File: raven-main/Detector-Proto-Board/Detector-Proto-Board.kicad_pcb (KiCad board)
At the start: 2 copper layers, 40.2 x 40.4 mm, 41 parts, among them IC1 ADA4817-1ARDZ-R7, J1 Conn_01x04, J2 Conn_01x01, J3 Conn_01x02, U9 TLV3201AIDCKT

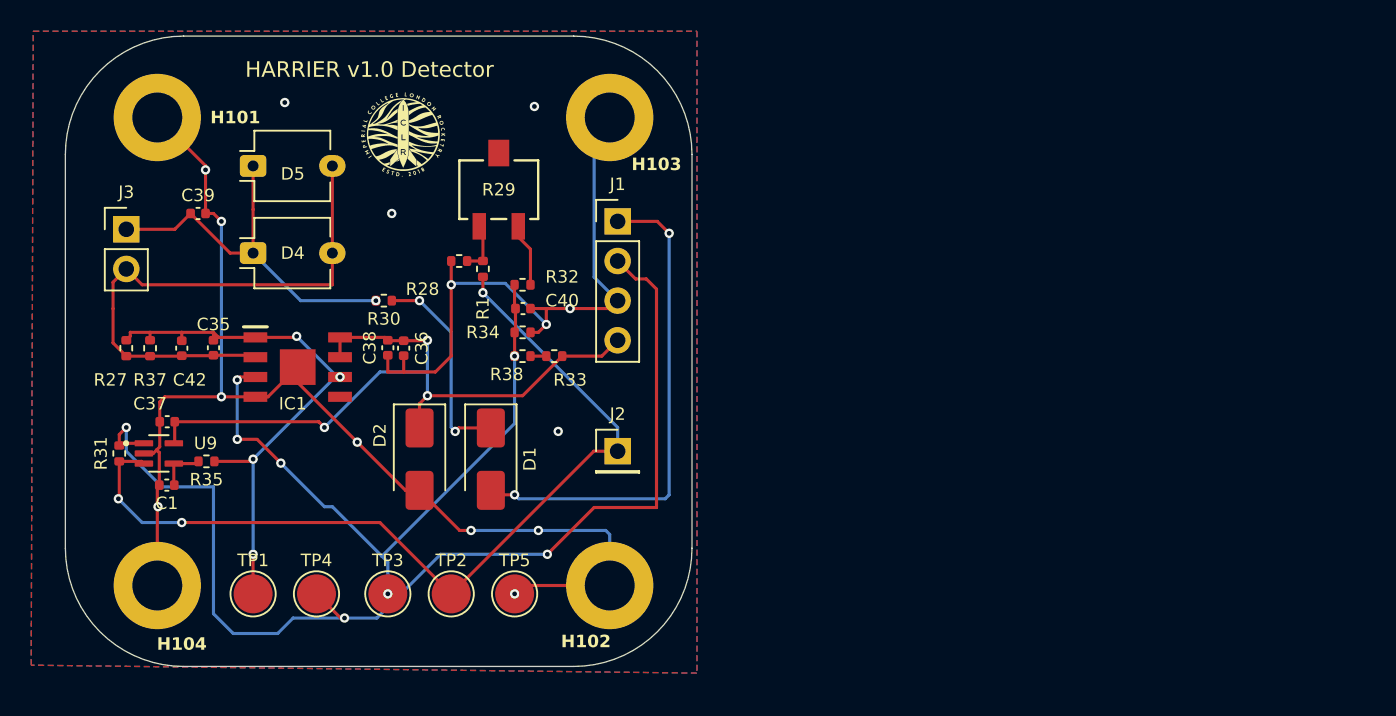
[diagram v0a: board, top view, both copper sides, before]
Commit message: Added 3.3V voltage divider to detector board
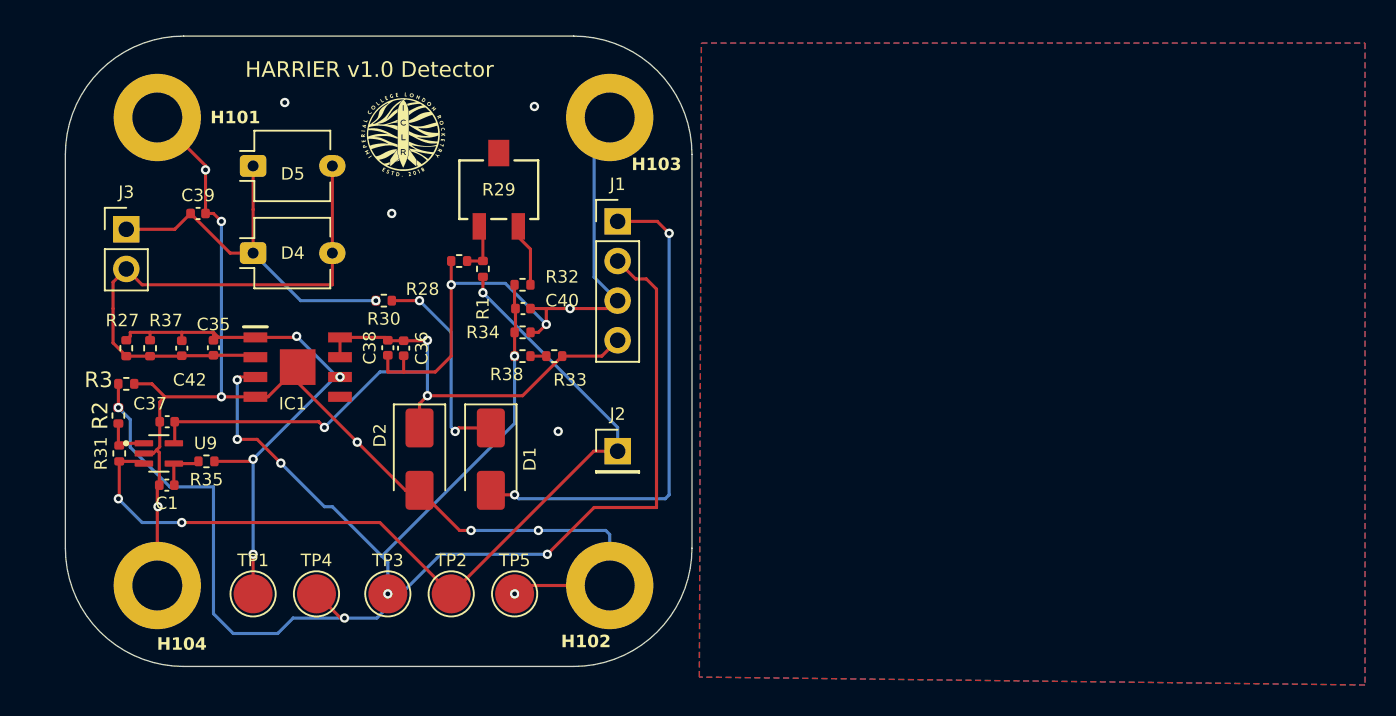
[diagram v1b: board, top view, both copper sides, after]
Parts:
- added R2: 1k, Resistor_SMD:R_0402_1005Metric, F.Cu at (95.5, 86.1)
- added R3: 2k, Resistor_SMD:R_0402_1005Metric, F.Cu at (96.0, 84.1)
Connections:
- R31 pad 2: /Detector_Out_A -> Net-(U9-OUT)
- U9 pad 1: /Detector_Out_A -> Net-(U9-OUT)
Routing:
- net Net-(U9-OUT): track 0.00 -> 3.07 mm
- net GND: track 117.5 -> 119.8 mm

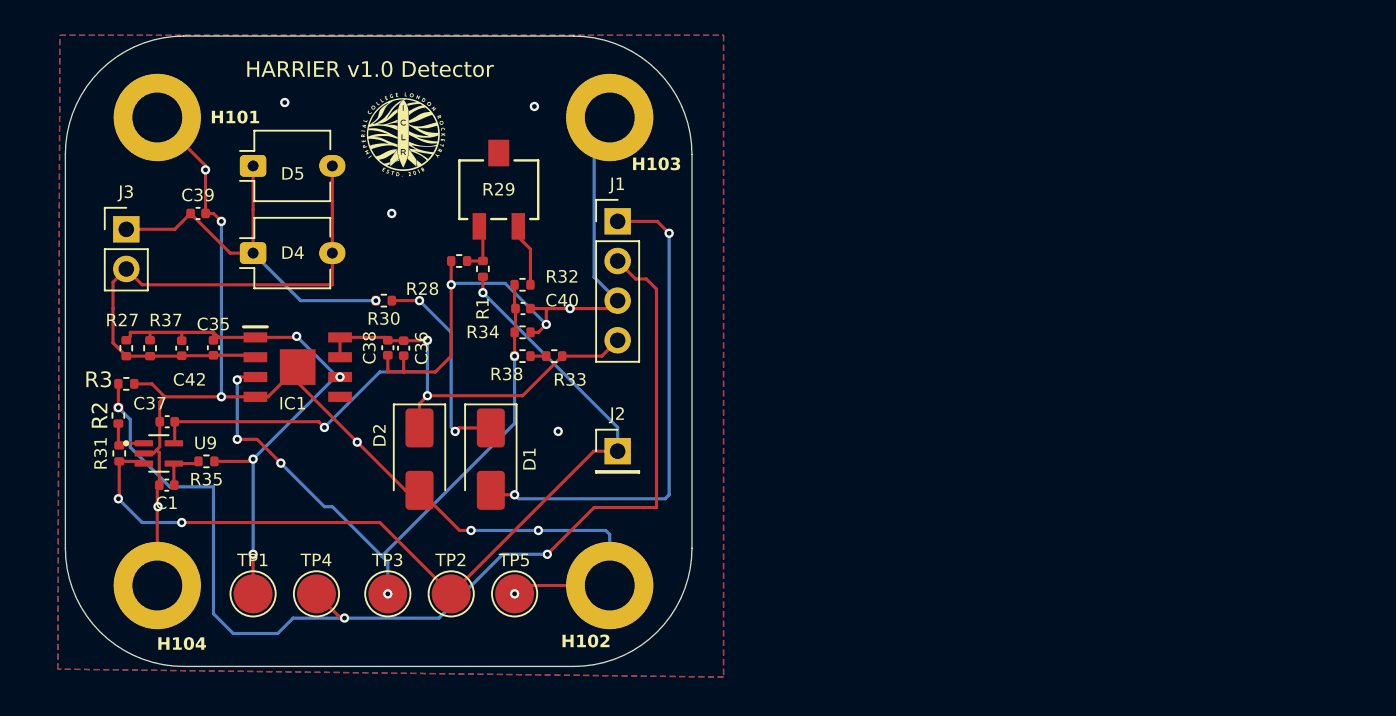
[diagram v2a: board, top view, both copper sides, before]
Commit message: Fixed grounding on proto board
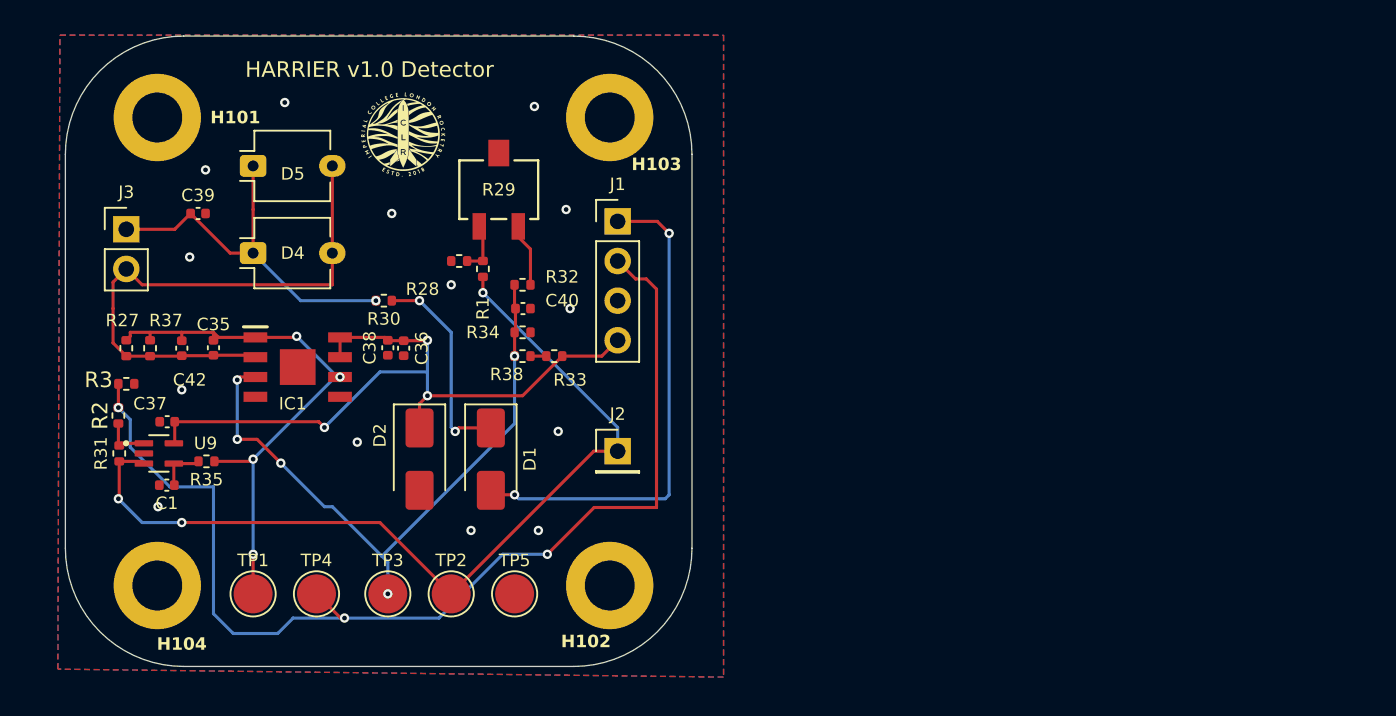
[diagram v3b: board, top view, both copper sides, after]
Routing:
- net GND: track 119.8 -> 2.07 mm, vias 15 -> 14
